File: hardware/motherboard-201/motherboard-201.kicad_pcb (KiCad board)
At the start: 2 copper layers, 216 x 150 mm, 124 parts, among them J1 PWR_conn, J2 DB25M, J3 MSX_Slot, J4 MSX_Slot, J5 GFX_Connector_Output, J6 CONN_JOY, J7 CONN_JOY, J8 DIN8, K1 Relay, Q1 2N2222, Q2 2N2907, SW1 Push_button, U1 62256, U10 74HC04, U11 74HC32, U12 74HC32, U13 74HC32, U14 74HC08, U15 74HC139, U16 74LS07, U17 74HC74, U18 74HCT08, U19 LM311, U2 62256, U20 SST39SF0, U21 74HC138, U22 74HC138, U23 74HC157, U24 AY-3-8910, U25 74HC157, U26 74HC138, U27 74HC153, U28 82C55A, U3 74HCT244, U4 74HCT244, U5 74HCT244, U6 Z84C00, U7 74HC74, U8 74HCT245, U9 74HCU04, Y1 3.58Mhz

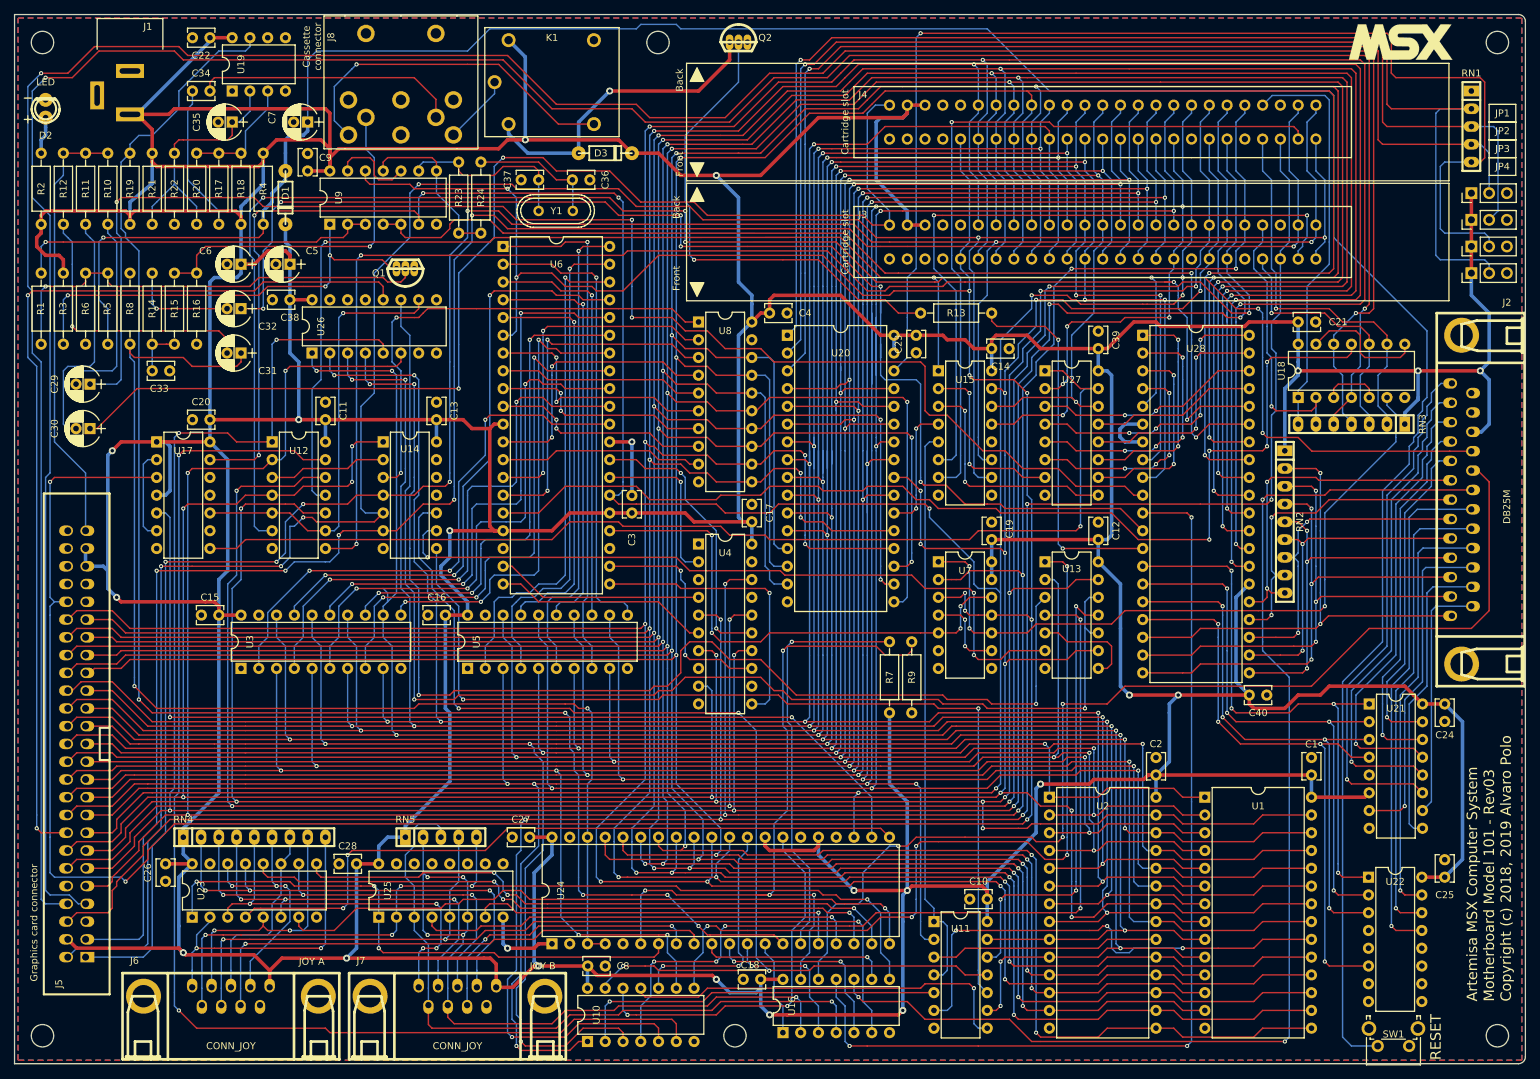
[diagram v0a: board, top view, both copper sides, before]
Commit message: Remove buffers from address and control bus
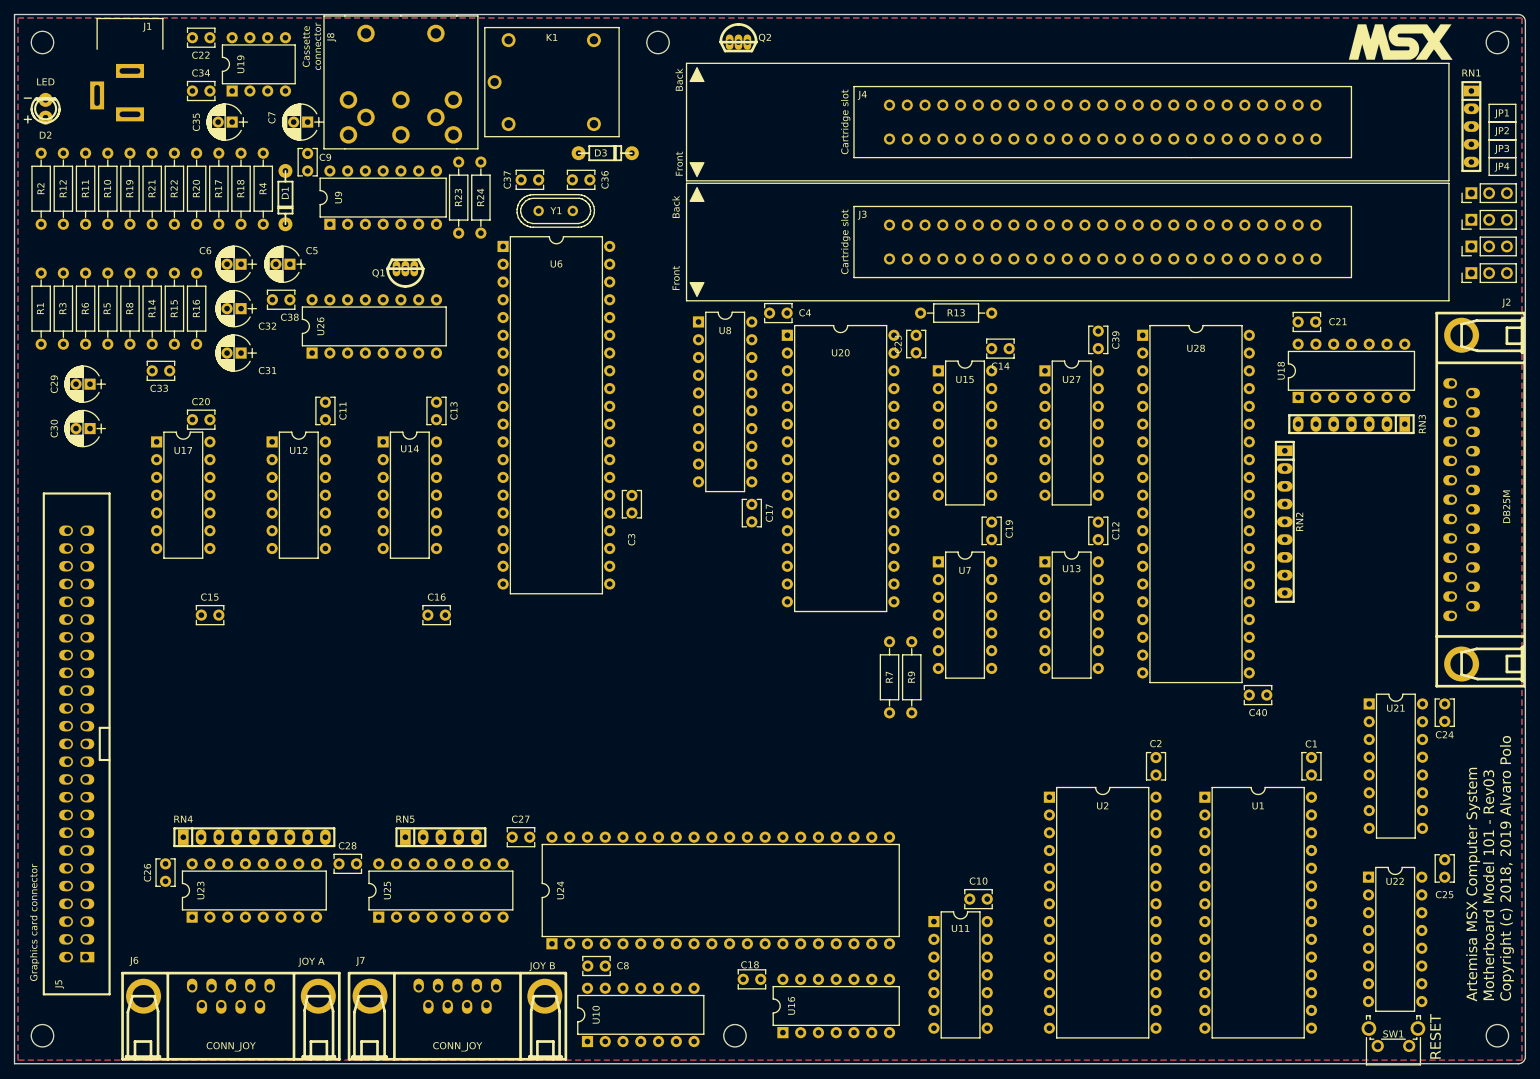
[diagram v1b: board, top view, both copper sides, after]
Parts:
- removed U3, U4, U5: 74HCT244, artemisa:DIP-20_300
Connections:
- U6 pad 1: /CPU/A11 -> /CPU/ADDR11
- U6 pad 19: Net-(U4-Pad4) -> /~MREQ
- U6 pad 2: /CPU/A12 -> /CPU/ADDR12
- U6 pad 20: Net-(U4-Pad6) -> /~IORQ
- U6 pad 21: Net-(U4-Pad11) -> /~RD
- U6 pad 22: Net-(U4-Pad13) -> /~WR
- U6 pad 27: Net-(U4-Pad2) -> /~M1
- U6 pad 28: Net-(U4-Pad15) -> /~RFSH
- U6 pad 3: /CPU/A13 -> /CPU/ADDR13
- U6 pad 30: /CPU/A0 -> /ADDR0
- U6 pad 31: /CPU/A1 -> /ADDR1
- U6 pad 32: /CPU/A2 -> /CPU/ADDR2
- U6 pad 33: /CPU/A3 -> /CPU/ADDR3
- U6 pad 34: /CPU/A4 -> /CPU/ADDR4
- U6 pad 35: /CPU/A5 -> /CPU/ADDR5
- U6 pad 36: /CPU/A6 -> /CPU/ADDR6
- U6 pad 37: /CPU/A7 -> /CPU/ADDR7
- U6 pad 38: /CPU/A8 -> /CPU/ADDR8
- U6 pad 39: /CPU/A9 -> /CPU/ADDR9
- U6 pad 4: /CPU/A14 -> /ADDR14
- U6 pad 40: /CPU/A10 -> /CPU/ADDR10
- U6 pad 5: /CPU/A15 -> /ADDR15
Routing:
- net ~: track 1471.7 -> 0.00 mm, vias 20 -> 0
- net /CPU/DATA6: track 595.6 -> 0.00 mm, vias 12 -> 0
- net /CPU/DATA4: track 593.5 -> 0.00 mm, vias 12 -> 0
- net /CPU/DATA3: track 577.3 -> 0.00 mm, vias 10 -> 0
- net /CPU/DATA5: track 576.8 -> 0.00 mm, vias 12 -> 0
- net /CPU/DATA7: track 575.1 -> 0.00 mm, vias 12 -> 0
- net /CPU/DATA2: track 547.7 -> 0.00 mm, vias 10 -> 0
- net /CPU/DATA0: track 539.4 -> 0.00 mm, vias 9 -> 0
- net /~RESET: track 535.4 -> 0.00 mm, vias 12 -> 0
- net /CPU/DATA1: track 531.1 -> 0.00 mm, vias 8 -> 0
- net /ADDR1: track 483.7 -> 0.00 mm, vias 11 -> 0
- net /CLK: track 457.2 -> 0.00 mm, vias 11 -> 0
- net /~RD: track 456.3 -> 0.00 mm, vias 15 -> 0
- net /ADDR0: track 432.3 -> 0.00 mm, vias 11 -> 0
- net /ADDR15: track 420.7 -> 0.00 mm, vias 11 -> 0
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
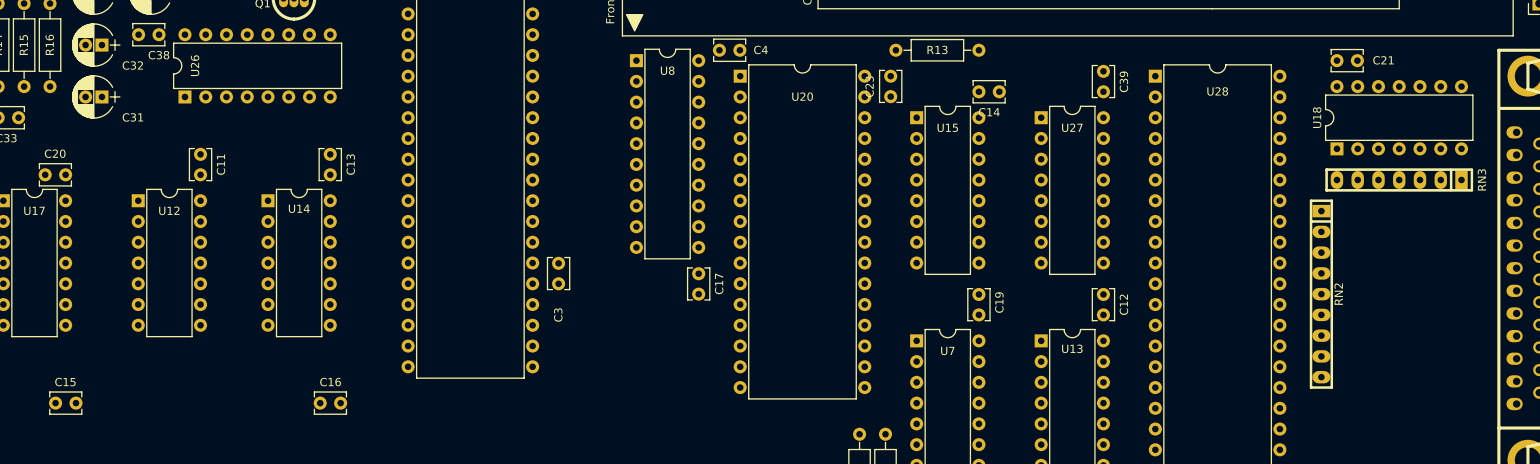
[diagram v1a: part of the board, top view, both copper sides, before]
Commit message: Assume open-drain outputs in INT and WAIT signals
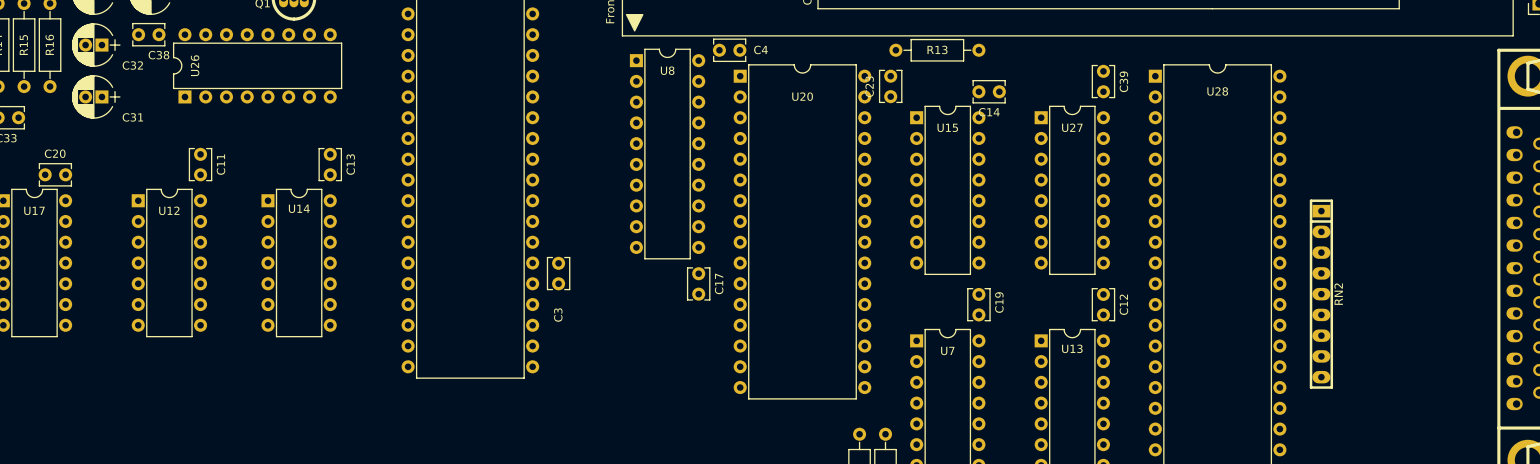
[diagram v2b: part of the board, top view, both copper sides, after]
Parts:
- removed C15, C16, C21: 100nF, artemisa:Disc_capacitor
- removed RN3: 10K, artemisa:RN6
- removed U18: 74HCT08, artemisa:DIP-14_300
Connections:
- J3 pad 7: /SLOTS/~EXTWAIT2 -> /~WAIT
- J3 pad 8: /SLOTS/~EXTINT2 -> /~INT
- J4 pad 7: /SLOTS/~EXTWAIT3 -> /~WAIT
- J4 pad 8: /SLOTS/~EXTINT3 -> /~INT
- J5 pad 7: /SLOTS/~VDPWAIT -> /~WAIT
- J5 pad 8: /SLOTS/~VDPINT -> /~INT
- U6 pad 16: /~EXTINT -> /~INT
- U7 pad 1: /~EXTWAIT -> /~WAIT
- U7 pad 10: /~EXTWAIT -> /~WAIT

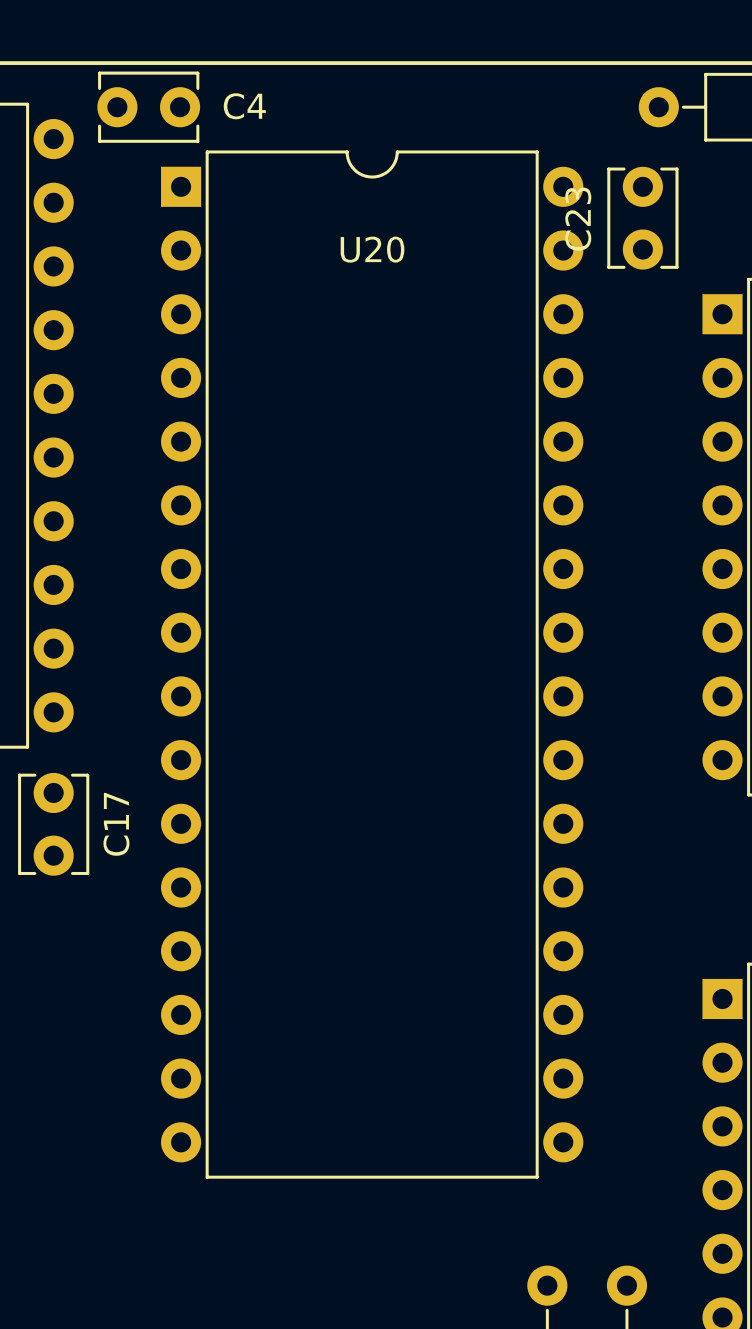
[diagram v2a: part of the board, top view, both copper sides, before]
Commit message: Reassociate footprint of ROM to PLCC32
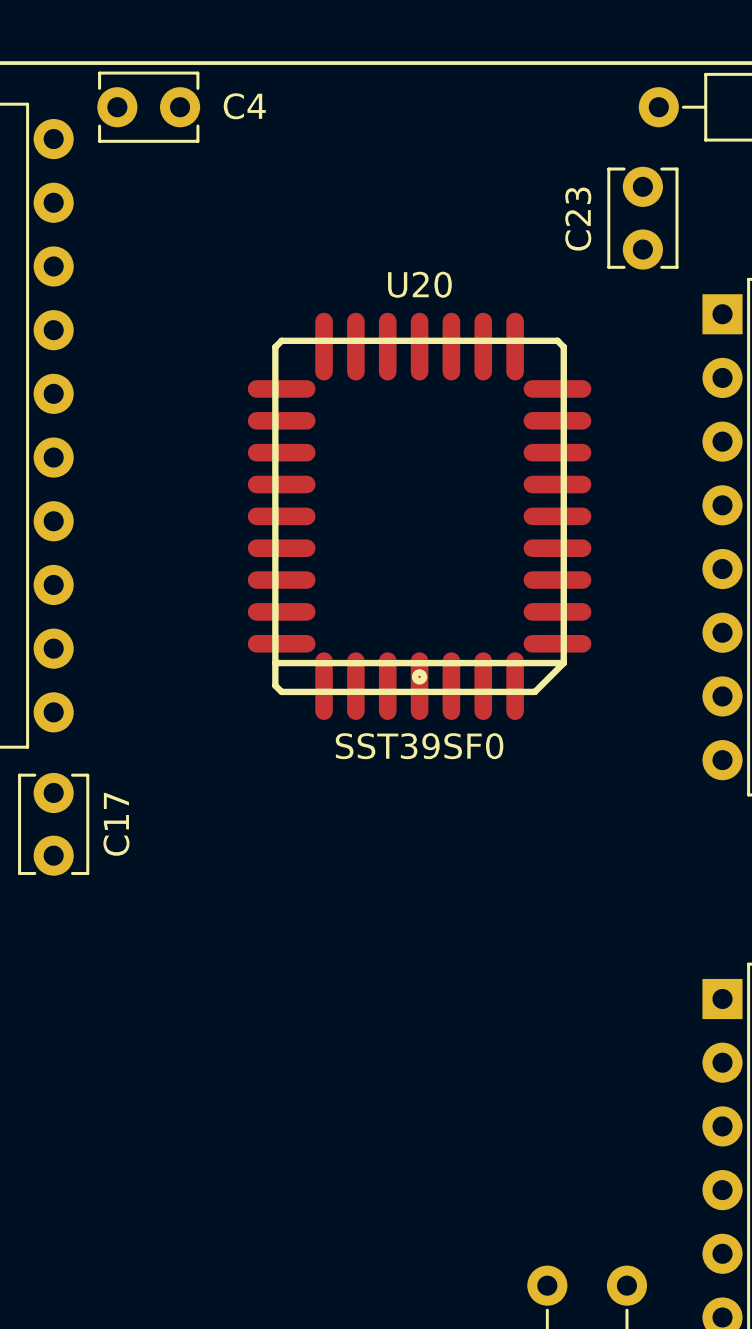
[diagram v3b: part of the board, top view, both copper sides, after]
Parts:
- U20: footprint artemisa:DIP-32_600 -> artemisa:PLCC32
- moved U20 16.2 mm to (176.9, 137.6)

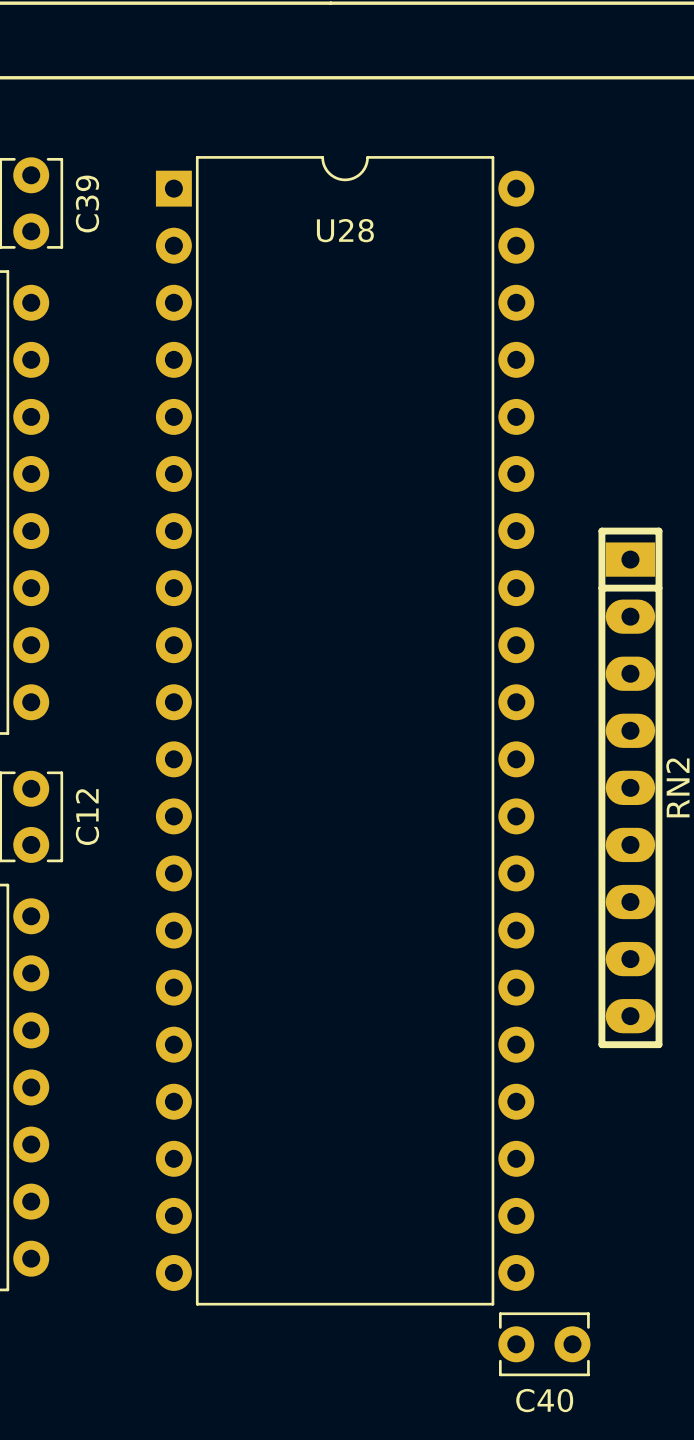
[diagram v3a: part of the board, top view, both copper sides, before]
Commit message: Use PLCC44 version of PPI
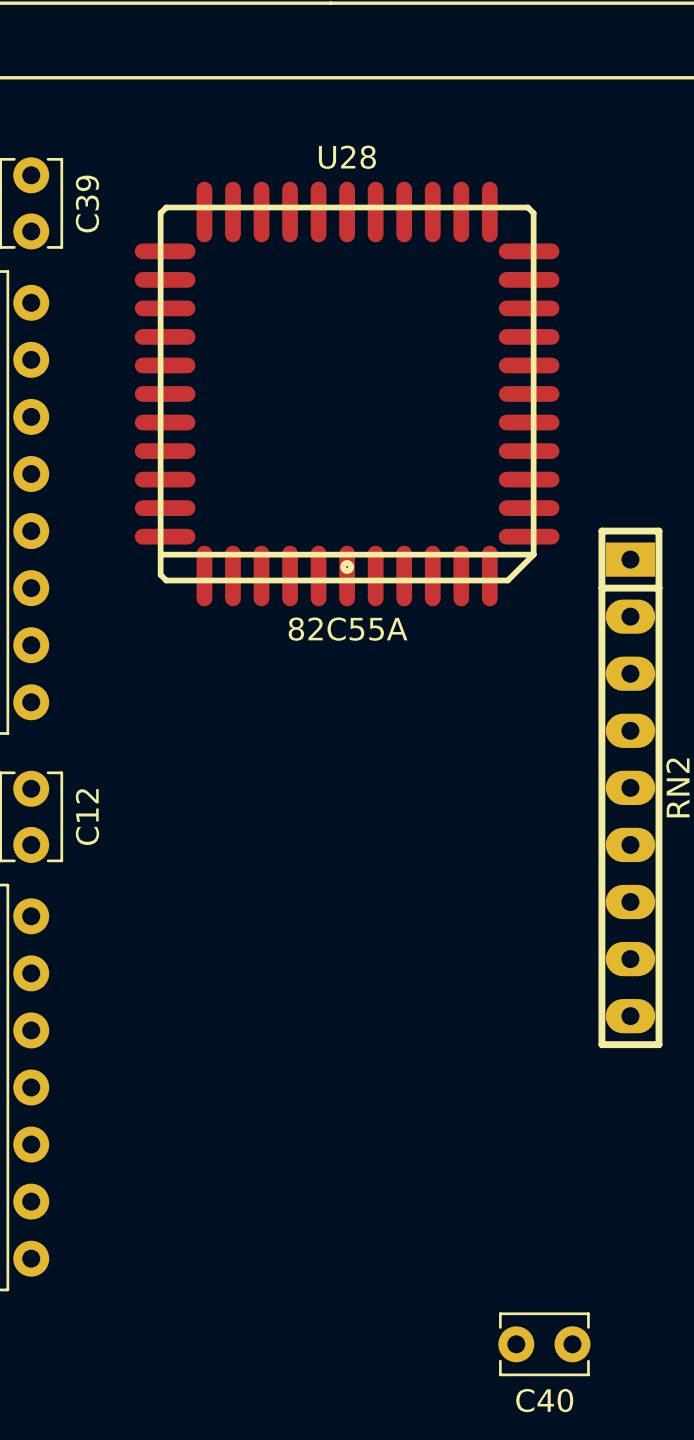
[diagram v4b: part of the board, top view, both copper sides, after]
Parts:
- U28: footprint artemisa:DIP-40_600 -> artemisa:PLCC44
- moved U28 12.0 mm to (225.9, 133.6)
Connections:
- U28 pad 1: /PPI/PA3 -> Net-(U28-Pad1)
- U28 pad 10: /BEEP -> /ADDR0
- U28 pad 11: /~CAPSLOCK -> /BEEP
- U28 pad 12: /CASOUT -> Net-(U28-Pad12)
- U28 pad 13: /~CASMOTOR -> /~CAPSLOCK
- U28 pad 14: /KBD/KBROW0 -> /CASOUT
- U28 pad 15: /KBD/KBROW1 -> /~CASMOTOR
- U28 pad 16: /KBD/KBROW2 -> /KBD/KBROW0
- U28 pad 17: /KBD/KBROW3 -> /KBD/KBROW1
- U28 pad 18: /KBD/KBCOL0 -> /KBD/KBROW2
- U28 pad 19: /KBD/KBCOL1 -> /KBD/KBROW3
- U28 pad 2: /PPI/PA2 -> /PPI/PA3
- U28 pad 20: /KBD/KBCOL2 -> /KBD/KBCOL0
- U28 pad 21: /KBD/KBCOL3 -> /KBD/KBCOL1
- U28 pad 22: /KBD/KBCOL4 -> /KBD/KBCOL2
- U28 pad 23: /KBD/KBCOL5 -> Net-(U28-Pad23)
- U28 pad 24: /KBD/KBCOL6 -> /KBD/KBCOL3
- U28 pad 25: /KBD/KBCOL7 -> /KBD/KBCOL4
- U28 pad 26: ~ -> /KBD/KBCOL5
- U28 pad 27: /CPU/DATA7 -> /KBD/KBCOL6
- U28 pad 28: /CPU/DATA6 -> /KBD/KBCOL7
- U28 pad 29: /CPU/DATA5 -> ~
- U28 pad 3: /PPI/PA1 -> /PPI/PA2
- U28 pad 30: /CPU/DATA4 -> /CPU/DATA7
- U28 pad 31: /CPU/DATA3 -> /CPU/DATA6
- U28 pad 32: /CPU/DATA2 -> /CPU/DATA5
- U28 pad 33: /CPU/DATA1 -> /CPU/DATA4
- U28 pad 34: /CPU/DATA0 -> Net-(U28-Pad34)
- U28 pad 35: /RESET -> /CPU/DATA3
- U28 pad 36: /~PPIWR -> /CPU/DATA2
- U28 pad 37: /PPI/PA7 -> /CPU/DATA1
- U28 pad 38: /PPI/PA6 -> /CPU/DATA0
- U28 pad 39: /PPI/PA5 -> /RESET
- U28 pad 4: /PPI/PA0 -> /PPI/PA1
- U28 pad 40: /PPI/PA4 -> /~PPIWR
- U28 pad 5: /~PPIRD -> /PPI/PA0
- U28 pad 6: GND -> /~PPIRD
- U28 pad 8: /ADDR1 -> GND
- U28 pad 9: /ADDR0 -> /ADDR1
